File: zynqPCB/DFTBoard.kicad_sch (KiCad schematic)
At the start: 0 parts

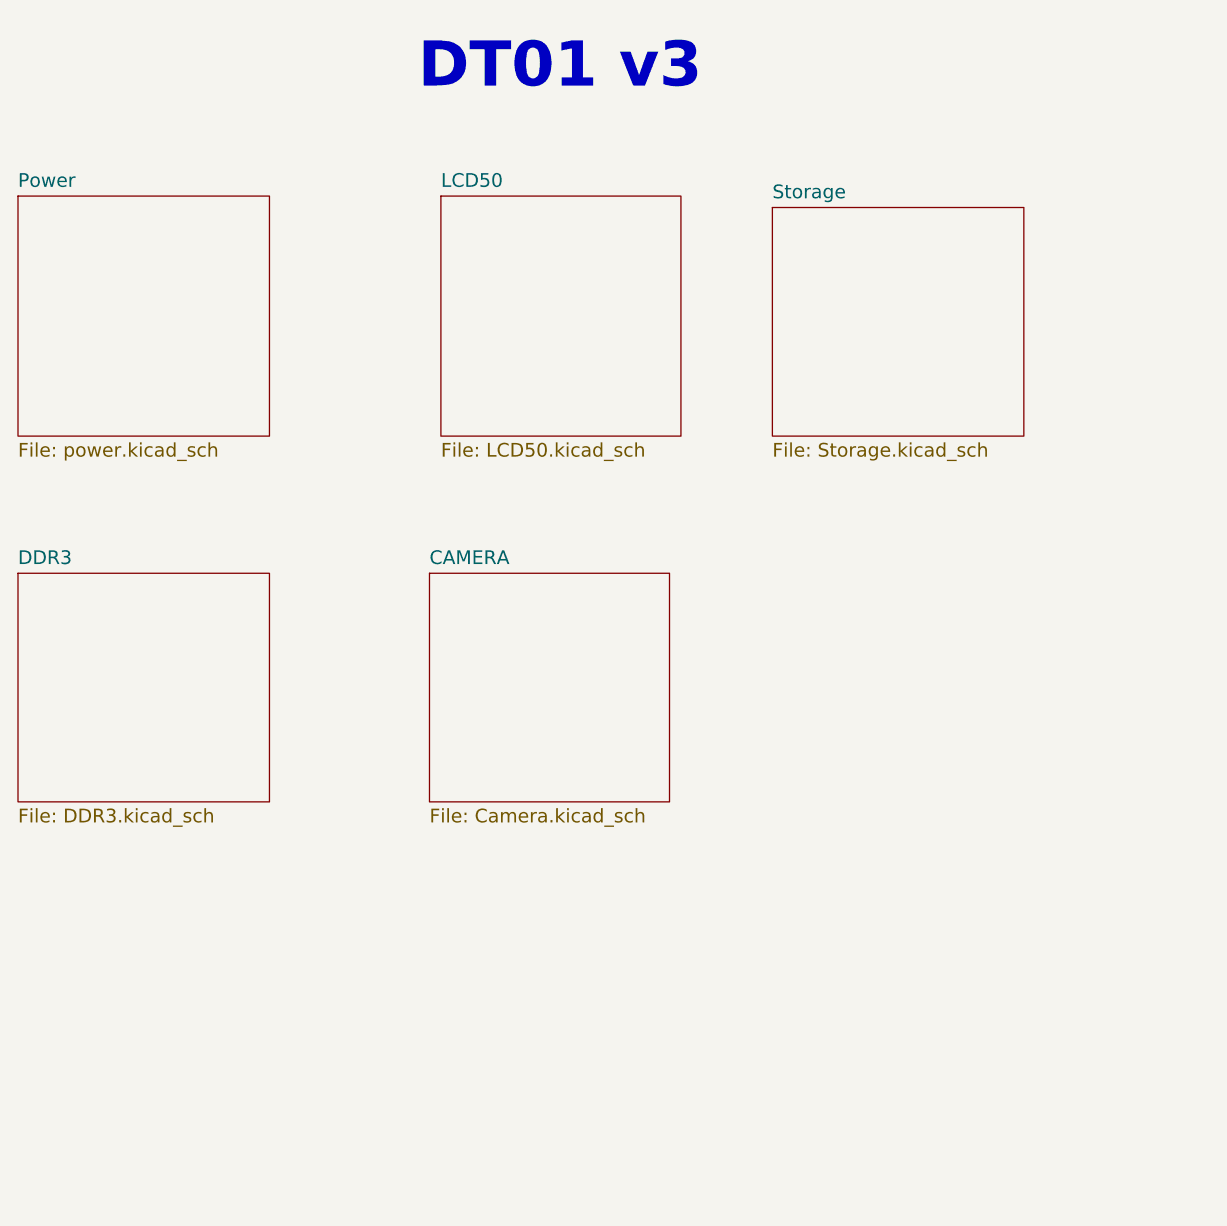
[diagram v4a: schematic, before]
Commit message: Sanity Checks and added some footprints
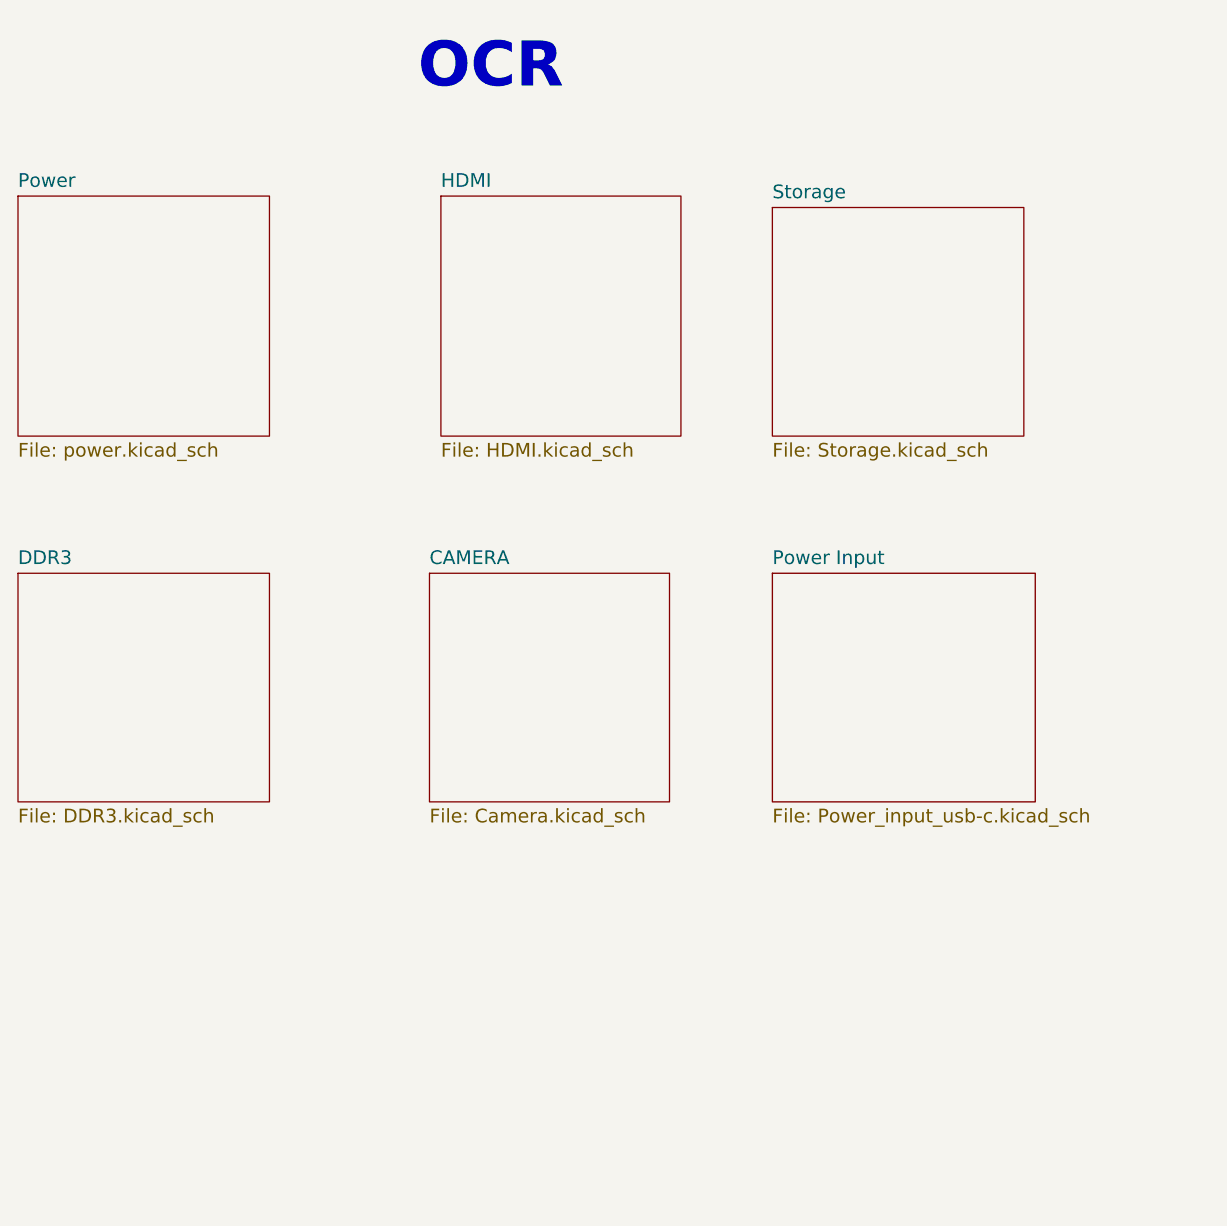
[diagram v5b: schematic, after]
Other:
- sheet LCD50 renamed HDMI
- added sheet Power Input (Power_input_usb-c.kicad_sch)
- sheet HDMI: file LCD50.kicad_sch -> HDMI.kicad_sch
- note added: "OCR"
- note removed: "DT01 v3"
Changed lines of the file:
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@@
 		)
 	)
-	(text "DT01 v3"
+	(text "OCR\n"
 		(exclude_from_sim no)
 		(at 134.62 39.37 0)
@@
 			(project "DFTBoard"
 				(path "/49eba173-d38c-4d05-b21c-b4a14c4948c2"
-					(page "4")
+					(page "3")
 				)
 			)
@@
 			(project "DFTBoard"
 				(path "/49eba173-d38c-4d05-b21c-b4a14c4948c2"
-					(page "8")
+					(page "7")
 				)
 			)
@@
 			(color 0 0 0 0)
 		)
-		(property "Sheetname" "LCD50"
+		(property "Sheetname" "HDMI"
 			(at 137.16 49.9614 0)
 			(show_name no)
@@
 			)
 		)
-		(property "Sheetfile" "LCD50.kicad_sch"
+		(property "Sheetfile" "HDMI.kicad_sch"
 			(at 137.16 78.1562 0)
 			(show_name no)
@@
 			(project "DFTBoard"
 				(path "/49eba173-d38c-4d05-b21c-b4a14c4948c2"
-					(page "7")
+					(page "4")
 				)
 			)
@@
 				)
 			)
+		)
+	)
+	(sheet
+		(at 173.99 92.71)
+		(size 29.21 25.4)
+		(exclude_from_sim no)
+		(in_bom yes)
+		(on_board yes)
+		(dnp no)
+		(fields_autoplaced yes)
+		(stroke
+			(width 0.1524)
+			(type solid)
+		)
+		(fill
+			(color 0 0 0 0)
+		)
+		(property "Sheetname" "Power Input"
+			(at 173.99 91.8714 0)
+			(show_name no)
+			(do_not_autoplace no)
+			(effects
+				(font
+					(size 1.524 1.524)
+				)
+				(justify left bottom)
+			)
+		)
+		(property "Sheetfile" "Power_input_usb-c.kicad_sch"
+			(at 173.99 118.7962 0)
+			(show_name no)
+			(do_not_autoplace no)
+			(effects
+				(font
+					(size 1.524 1.524)
+				)
+				(justify left top)
+			)
+		)
+		(instances
+			(project "DFTBoard"
+				(path "/49eba173-d38c-4d05-b21c-b4a14c4948c2"
+					(page "2")
+				)
+			)
